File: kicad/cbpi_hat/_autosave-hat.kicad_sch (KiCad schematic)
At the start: 30 parts, among them J1 GPIO, J2 Screw_Terminal_01x02, Q1 HY15P03C2, U1 CAT24C256, U2 EUP3453WIR1

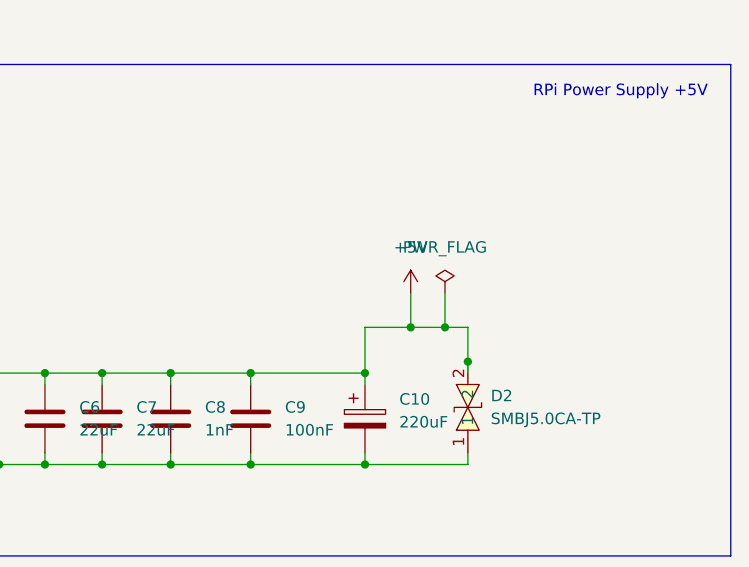
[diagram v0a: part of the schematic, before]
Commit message: 5V DC-DC converter is largely routed including reverse polarity protection
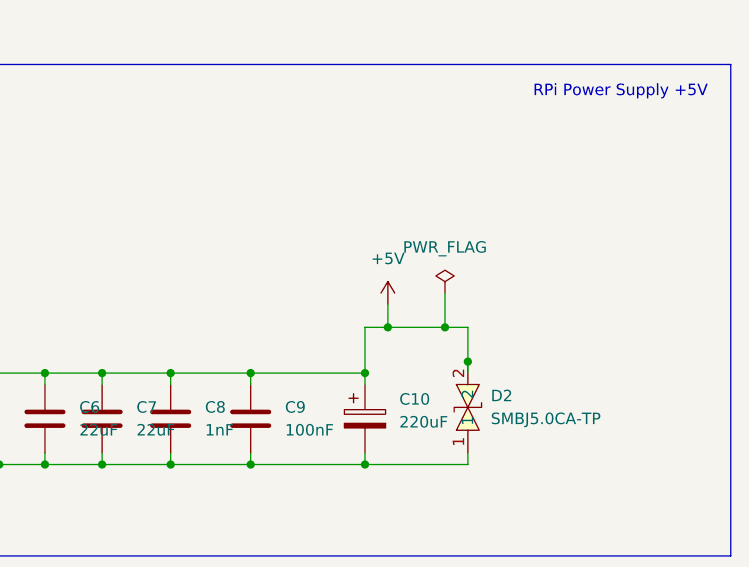
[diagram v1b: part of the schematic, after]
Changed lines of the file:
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@@
   (junction (at 422.91 63.5) (diameter 0) (color 0 0 0 0)
   )
+  (junction (at 541.02 48.26) (diameter 0) (color 0 0 0 0)
+  )
   (junction (at 420.37 63.5) (diameter 0) (color 0 0 0 0)
   )
@@
   )
   (junction (at 101.6 177.8) (diameter 1.016) (color 0 0 0 0)
-  )
-  (junction (at 543.56 48.26) (diameter 0) (color 0 0 0 0)
   )
   (junction (at 516.89 53.34) (diameter 0) (color 0 0 0 0)
@@
     (stroke (width 0) (type default) (color 0 0 0 0))
   )
-  (wire (pts (xy 547.37 48.26) (xy 543.56 48.26))
-    (stroke (width 0) (type default) (color 0 0 0 0))
-  )
   (polyline (pts (xy 292.1 12.7) (xy 292.1 53.34))
     (stroke (width 0) (type default) (color 0 0 0 0))
@@
     (stroke (width 0) (type solid) (color 0 0 0 0))
   )
+  (wire (pts (xy 541.02 45.72) (xy 541.02 48.26))
+    (stroke (width 0) (type default) (color 0 0 0 0))
+  )
   (wire (pts (xy 482.6 34.29) (xy 486.41 34.29))
     (stroke (width 0) (type default) (color 0 0 0 0))
@@
     (stroke (width 0) (type default) (color 0 0 0 0))
   )
-  (wire (pts (xy 538.48 48.26) (xy 543.56 48.26))
+  (wire (pts (xy 538.48 48.26) (xy 541.02 48.26))
     (stroke (width 0) (type default) (color 0 0 0 0))
   )
@@
     (stroke (width 0) (type default) (color 0 0 0 0))
   )
-  (wire (pts (xy 543.56 48.26) (xy 543.56 44.45))
-    (stroke (width 0) (type default) (color 0 0 0 0))
-  )
   (wire (pts (xy 31.75 66.04) (xy 60.96 66.04))
     (stroke (width 0) (type solid) (color 0 0 0 0))
@@
   )
   (wire (pts (xy 426.72 36.83) (xy 426.72 63.5))
+    (stroke (width 0) (type default) (color 0 0 0 0))
+  )
+  (wire (pts (xy 541.02 48.26) (xy 547.37 48.26))
     (stroke (width 0) (type default) (color 0 0 0 0))
   )
@@
     (pin "2")
   )
-  (symbol (lib_id "power:+5V") (at 543.56 44.45 0) (unit 1)
-    (in_bom yes) (on_board yes) (fields_autoplaced)
-    (property "Reference" "#PWR0104" (id 0) (at 543.56 48.26 0)
-      (effects (font (size 1.27 1.27)) hide)
-    )
-    (property "Value" "+5V" (id 1) (at 543.56 39.37 0))
-    (property "Footprint" "" (id 2) (at 543.56 44.45 0)
-      (effects (font (size 1.27 1.27)) hide)
-    )
-    (property "Datasheet" "" (id 3) (at 543.56 44.45 0)
-      (effects (font (size 1.27 1.27)) hide)
-    )
-    (pin "1")
-  )
   (symbol (lib_id "Device:C") (at 502.92 58.42 0) (unit 1)
     (in_bom yes) (on_board yes) (fields_autoplaced)
@@
     (pin "2")
   )
+  (symbol (lib_id "power:+5V") (at 541.02 45.72 0) (unit 1)
+    (in_bom yes) (on_board yes) (fields_autoplaced)
+    (property "Reference" "#PWR?" (id 0) (at 541.02 49.53 0)
+      (effects (font (size 1.27 1.27)) hide)
+    )
+    (property "Value" "+5V" (id 1) (at 541.02 40.64 0))
+    (property "Footprint" "" (id 2) (at 541.02 45.72 0)
+      (effects (font (size 1.27 1.27)) hide)
+    )
+    (property "Datasheet" "" (id 3) (at 541.02 45.72 0)
+      (effects (font (size 1.27 1.27)) hide)
+    )
+    (pin "1")
+  )
   (symbol (lib_id "smbj5.0ca-tp:SMBJ5.0CA-TP") (at 549.91 57.15 90) (unit 1)
     (in_bom yes) (on_board yes) (fields_autoplaced)
@@
       (reference "#PWR0103") (unit 1) (value "+3.3V") (footprint "")
     )
-    (path "/3d7416f9-5d37-4c61-aaef-471c18c3e7d3"
-      (reference "#PWR0104") (unit 1) (value "+5V") (footprint "")
-    )
     (path "/e1143864-b5ce-4375-b69b-b626f77fe8a4"
       (reference "#PWR0105") (unit 1) (value "GND") (footprint "")
@@
       (reference "#PWR0108") (unit 1) (value "+24V") (footprint "")
     )
+    (path "/dd7b3fef-a362-4f7c-a087-1e8e9a911fa1"
+      (reference "#PWR?") (unit 1) (value "+5V") (footprint "")
+    )
     (path "/0f7872a7-de47-41d5-a21f-9934102d3a5f"
